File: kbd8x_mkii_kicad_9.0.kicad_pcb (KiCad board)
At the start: 2 copper layers, 343.7 x 118.3 mm, 196 parts, among them J1 AVR-ISP-6, SW1 SW_Push, U1 ATmega32U4-A, U2 PRTR5V0U2X, Y1 16MHz

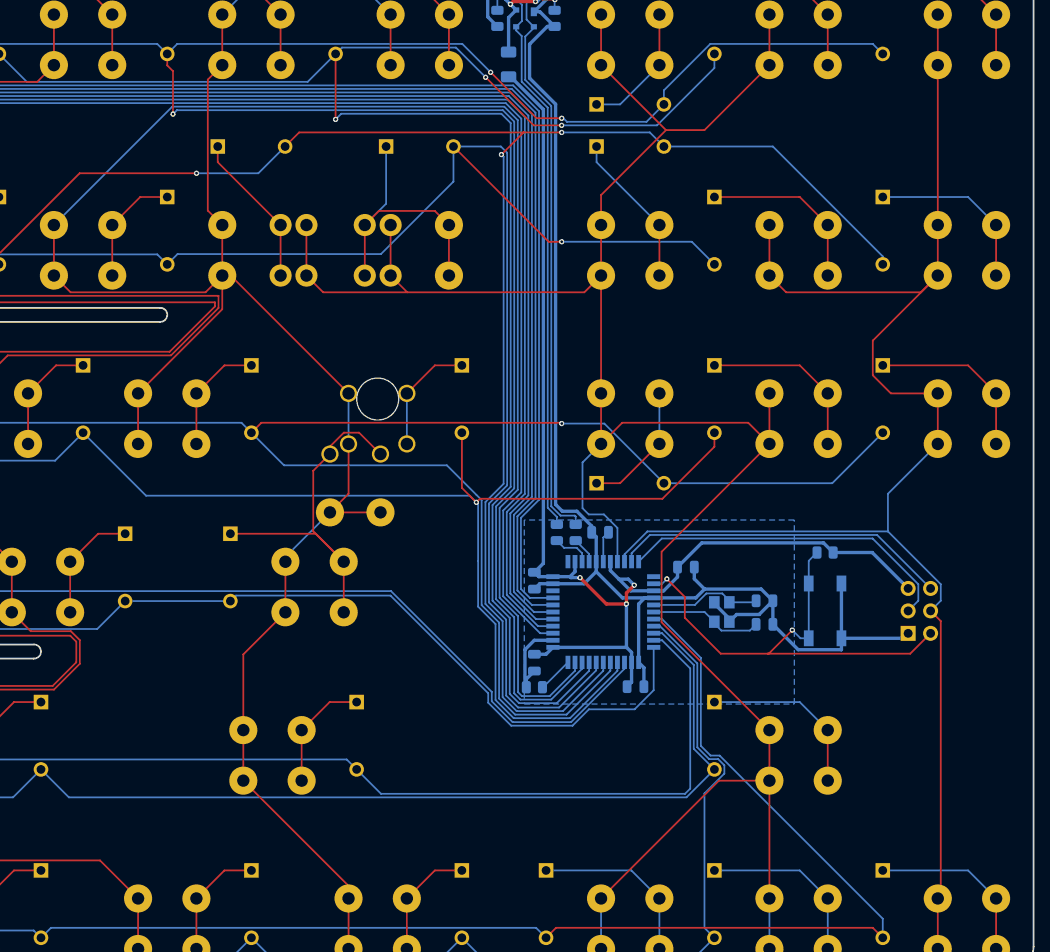
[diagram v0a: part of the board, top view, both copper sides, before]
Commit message: Revisions to make workable PCB and push before experimenting with some row and column adjustment to attempt to clean up traces.
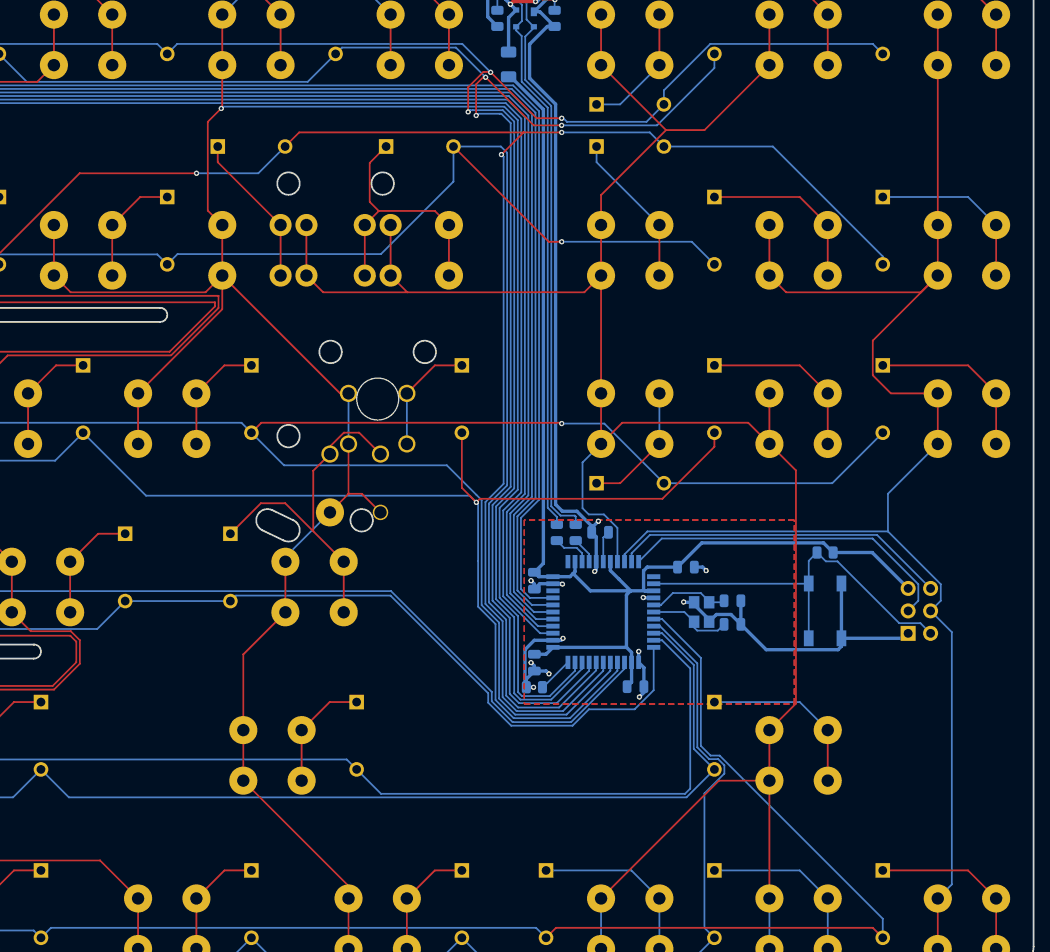
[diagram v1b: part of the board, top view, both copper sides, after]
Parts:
- moved C6 3.62 mm to (418.0, 269.7)
- moved C7 3.62 mm to (418.0, 267.1)
- moved Y1 2.29 mm to (414.5, 268.3)
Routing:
- net ROW0: track 446.4 -> 411.9 mm
- net COL6: track 338.7 -> 313.1 mm, vias 0 -> 1
- net GND: track 190.9 -> 168.8 mm, vias 0 -> 13
- net ROW1: track 379.8 -> 361.2 mm
- net RESET: track 53.6 -> 44.3 mm, vias 2 -> 0
- net COL7: track 265.3 -> 257.7 mm
- net XTAL2: track 12.7 -> 9.09 mm
- net XTAL1: track 12.9 -> 9.51 mm
- net Net-(D42-A): track 42.5 -> 40.5 mm
- net Net-(D28-A): track 32.2 -> 30.8 mm
- net COL8: track 178.9 -> 179.9 mm
- net +5V: track 137.8 -> 137.6 mm, vias 3 -> 0
- added copper zone on F.Cu, net GND
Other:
- outline, holes or cut-outs redrawn
